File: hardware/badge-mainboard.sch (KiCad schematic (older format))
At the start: 34 parts, among them J1 Vin, J3 Rpi_02x20_WaveShareEPD, J4 I2C_HEADER, J5 I2C_HEADER, SW1 User Button 2, SW2 User Button 1, SW3 User Button 3, SW4 User Button 4, U1 LM1117-3.3, U2 sensor-module-board

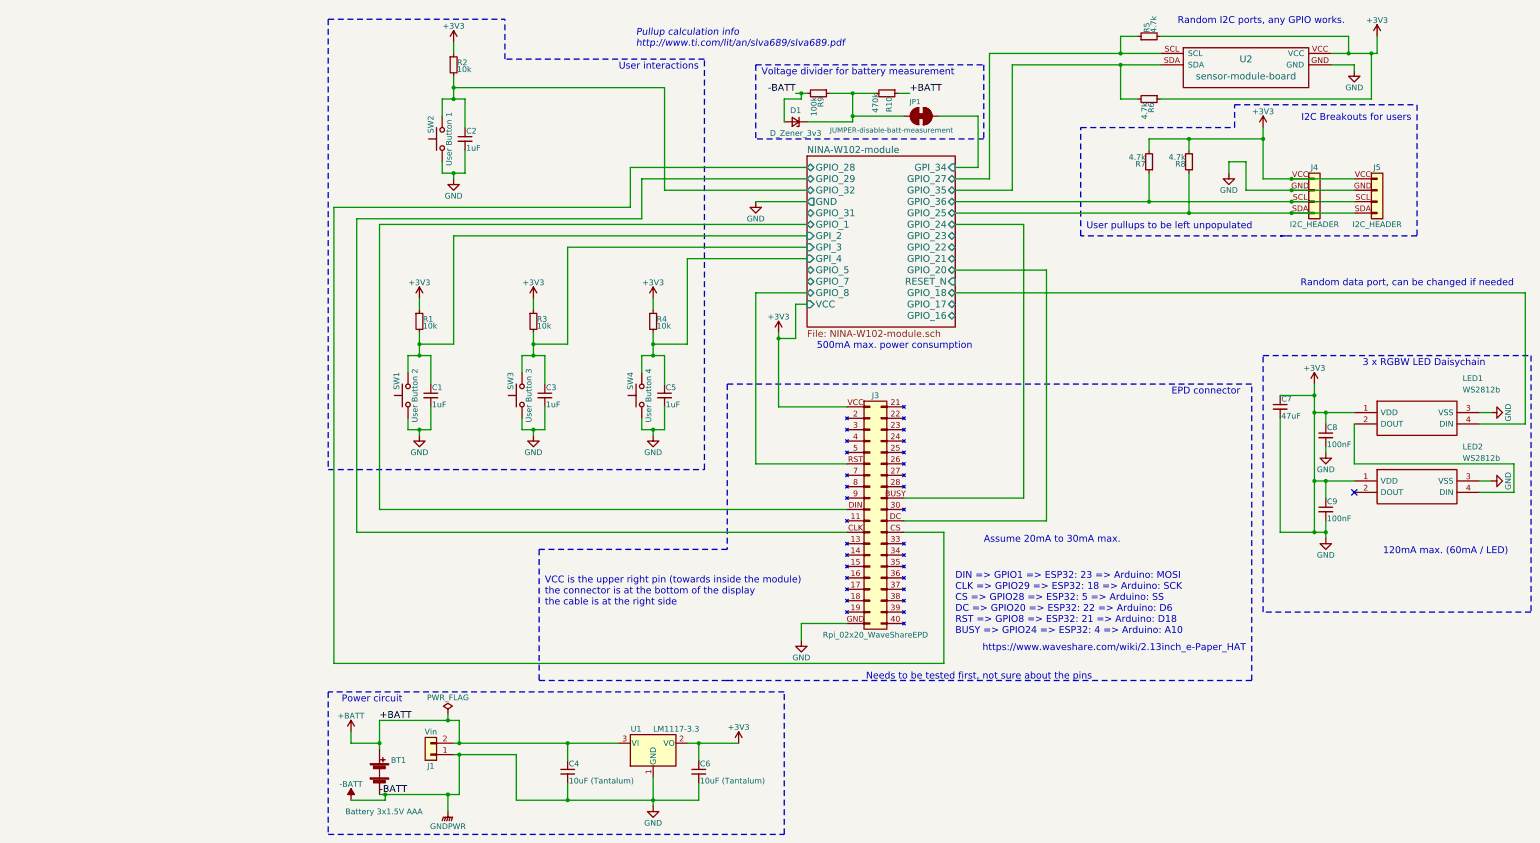
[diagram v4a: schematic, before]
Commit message: Fix 3v3 to GND connection on `ws28b`
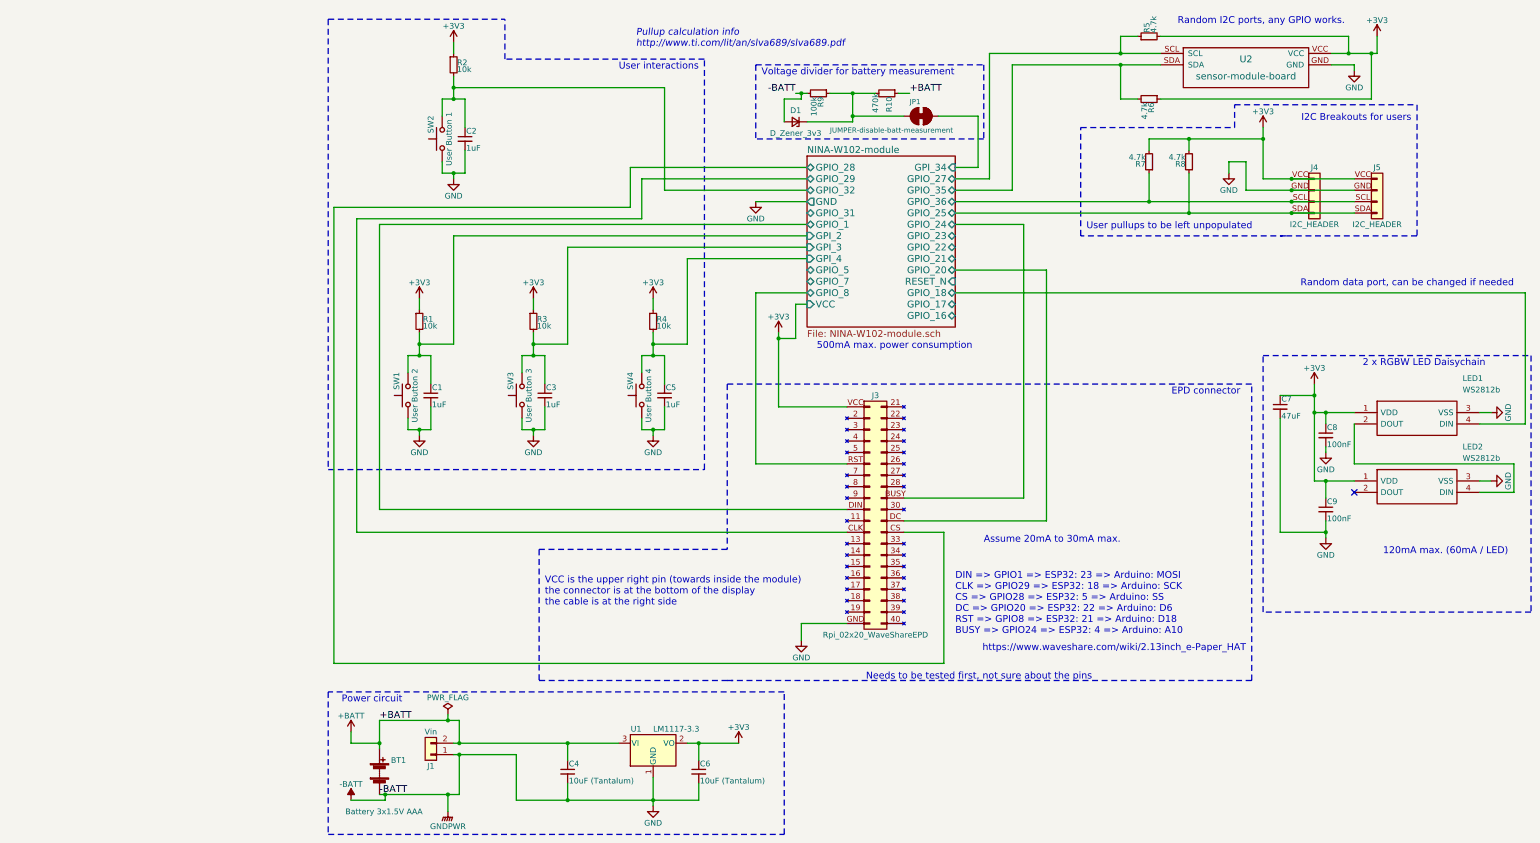
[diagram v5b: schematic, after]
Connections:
- net +3V3: no longer BT1.2 (-), C1.2, C2.2, C3.2, C4.2, C5.2, C6.2, C7.2, C8.2, C9.2, D1.2 (A), J1.1 (Pin_1), J3.GND (Pin_20), J4.GND, J5.GND, LED1.3 (VSS), LED2.3 (VSS), R9.2, SW1.1, SW2.1, SW3.1, SW4.1, U1.1 (GND), U2.GND
- new net -BATT: BT1.2 (-), C1.2, C2.2, C3.2, C4.2, C5.2, C6.2, C7.2, C8.2, C9.2, D1.2 (A), J1.1 (Pin_1), J3.GND (Pin_20), J4.GND, J5.GND, LED1.3 (VSS), LED2.3 (VSS), R9.2, SW1.1, SW2.1, SW3.1, SW4.1, U1.1 (GND), U2.GND
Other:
- note added: "2 x RGBW LED Daisychain"
- note removed: "3 x RGBW LED Daisychain"
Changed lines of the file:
@@
 LIBS:badgeComponents
 LIBS:badge-mainboard-cache
-EELAYER 25 0
+EELAYER 26 0
 EELAYER END
 $Descr A4 11693 8268
@@
 $EndComp
 Text Notes 10750 3600 2    60   ~ 0
-3 x RGBW LED Daisychain
+2 x RGBW LED Daisychain
 Text Notes 8050 600  0    60   ~ 0
 Random I2C ports, any GPIO works.
@@
 	9250 4600 9600 4600
 Connection ~ 9250 4000
-Connection ~ 9250 4600
 Wire Wire Line
 	9350 4300 9350 4350
@@
 	9600 950  9600 1000
 Wire Wire Line
-	9800 700  9800 850
-Wire Wire Line
-	9800 850  9400 850
+	9800 850  9800 700
+Wire Wire Line
+	9400 850  9800 850
 Wire Wire Line
 	6400 850  7900 850
@@
 	1700 6900 3150 6900
 Wire Wire Line
-	1750 6900 1750 6700
-Wire Wire Line
-	1750 6700 1050 6700
+	1750 6700 1750 6900
+Wire Wire Line
+	1050 6700 1750 6700
 Connection ~ 1750 6900
 Wire Notes Line
@@
 	8950 5050 9350 5050
 Wire Wire Line
-	9250 3750 9250 5050
+	9250 3750 9250 4600
 Wire Wire Line
 	9350 4950 9350 5100
@@
 Wire Wire Line
 	8950 4050 8950 5050
-Connection ~ 9250 5050
 Wire Wire Line
 	6100 2750 6900 2750
@@
 	1600 1250 1800 1250
 Wire Wire Line
-	1700 1250 1700 1050
+	1700 1050 1700 1250
 Wire Wire Line
 	1800 1250 1800 1500
@@
 	1300 3500 1500 3500
 Wire Wire Line
-	1400 3500 1400 3300
+	1400 3300 1400 3500
 Wire Wire Line
 	1500 3500 1500 3750
@@
 	2300 3500 2500 3500
 Wire Wire Line
-	2400 3500 2400 3300
+	2400 3300 2400 3500
 Wire Wire Line
 	2500 3500 2500 3750
@@
 	3350 3500 3550 3500
 Wire Wire Line
-	3450 3500 3450 3300
+	3450 3300 3450 3500
 Wire Wire Line
 	3550 3500 3550 3750
@@
 	5600 1200 5700 1200
 Wire Wire Line
-	4800 1200 4700 1200
+	4700 1200 4800 1200
 Wire Notes Line
 	4350 950  4350 1600

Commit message: Added diode and cleanedup shematic
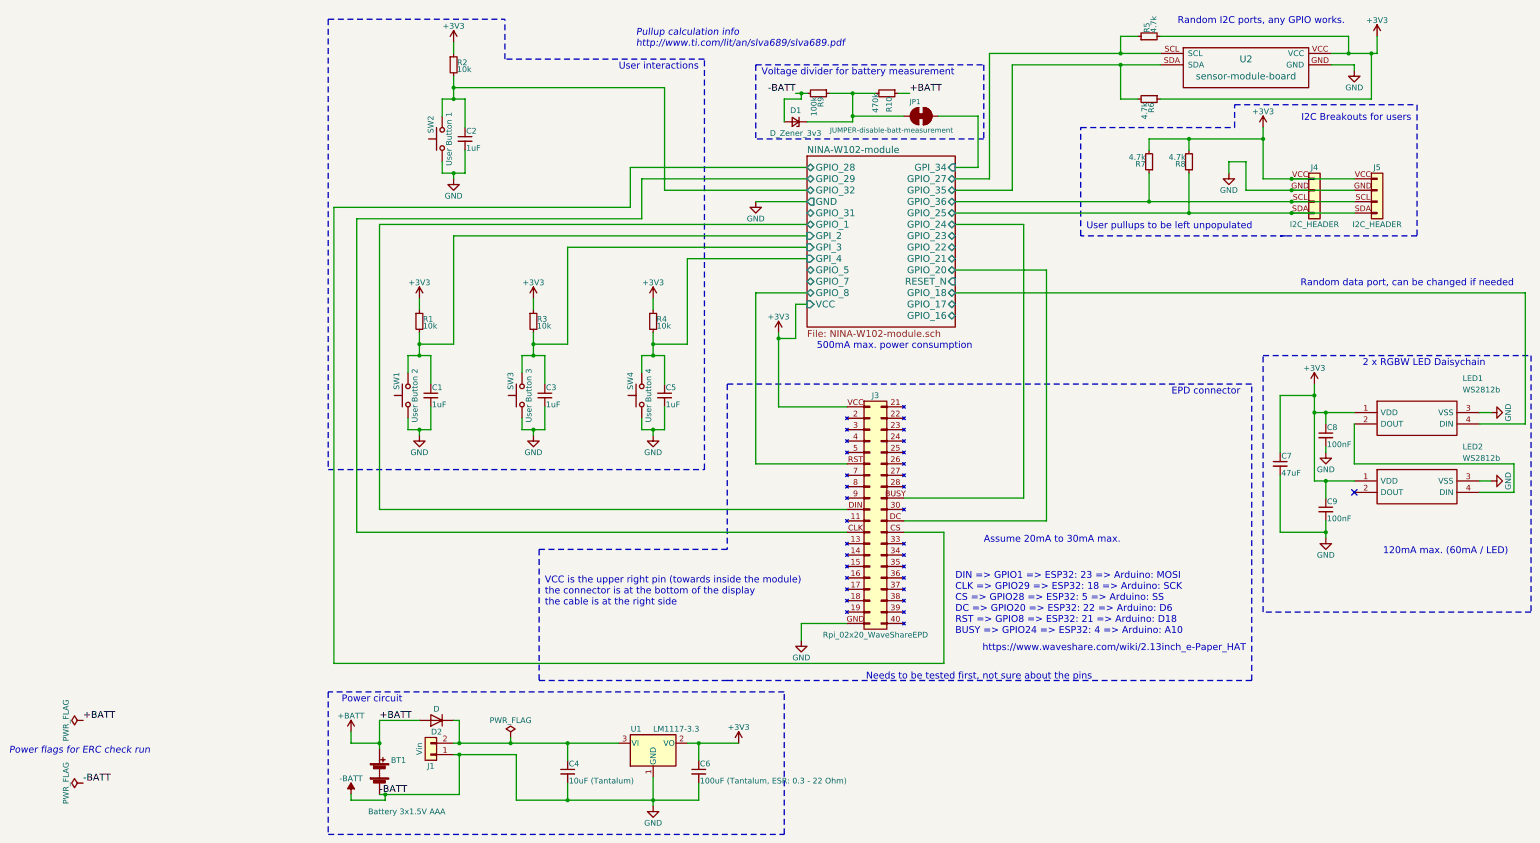
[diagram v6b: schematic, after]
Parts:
- added D2: D, Diodes_SMD:D_1206, symbol D
- C1, C2, C3, C5, C7, C8, C9: footprint Capacitors_SMD:C_1206 -> Capacitors_SMD:C_1206_HandSoldering
- C4: footprint Capacitors_SMD:C_1206 -> Capacitors_Tantalum_SMD:CP_Tantalum_Case-C_EIA-6032-28_Hand
- C6: value 10uF (Tantalum) -> 100uF (Tantalum, ESR: 0.3 - 22 Ohm); footprint Capacitors_SMD:C_1206 -> Capacitors_Tantalum_SMD:CP_Tantalum_Case-C_EIA-6032-28_Hand
- R1, R10, R2, R3, R4, R5, R6, R9: footprint Resistors_SMD:R_1206 -> Resistors_SMD:R_1206_HandSoldering
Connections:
- net +BATT: now also D2.2 (A); no longer C4.1, J1.2 (Pin_2), U1.3 (VI)
- new net: C4.1, D2.1 (K), J1.2 (Pin_2), U1.3 (VI)
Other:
- note added: "Power flags for ERC check run"
- moved on the sheet: C7

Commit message: Added comments for BOM
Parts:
- C4: Description (none) -> Tantalum
- C6: Description (none) -> Tantalum with ESR between 0.3 Ohm and 22 Ohm
- R7, R8: Description (none) -> User pullups, leave unpopulated
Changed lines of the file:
@@
 F 2 "Resistors_SMD:R_1206_HandSoldering" H 7800 1800 50  0001 C CNN
 F 3 "" H 7800 1800 50  0001 C CNN
+F 4 "User pullups, leave unpopulated" H 7800 1800 60  0001 C CNN "Description"
 	1    7800 1800
 	-1   0    0    1
@@
 F 2 "Resistors_SMD:R_1206_HandSoldering" H 8150 1800 50  0001 C CNN
 F 3 "" H 8150 1800 50  0001 C CNN
+F 4 "User pullups, leave unpopulated" H 8150 1800 60  0001 C CNN "Description"
 	1    8150 1800
 	-1   0    0    1
@@
 F 2 "Capacitors_Tantalum_SMD:CP_Tantalum_Case-C_EIA-6032-28_Hand" H 2700 7150 50  0001 C CNN
 F 3 "" H 2700 7150 50  0001 C CNN
+F 4 "Tantalum" H 2700 7150 60  0001 C CNN "Description"
 	1    2700 7150
 	1    0    0    -1
@@
 F 2 "Capacitors_Tantalum_SMD:CP_Tantalum_Case-C_EIA-6032-28_Hand" H 3850 7150 50  0001 C CNN
 F 3 "" H 3850 7150 50  0001 C CNN
+F 4 "Tantalum with ESR between 0.3 Ohm and 22 Ohm" H 3850 7150 60  0001 C CNN "Description"
 	1    3850 7150
 	1    0    0    -1

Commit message: added some more comments
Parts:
- J4, J5: Description (none) -> Leave unpopulated
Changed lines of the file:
@@
 F 2 "badgeComponents:I2C_HEADER_1X04_LOCK_LONGPADS" H 9250 2050 50  0001 C CNN
 F 3 "" H 9250 2050 50  0001 C CNN
+F 4 "Leave unpopulated" H 9250 2050 60  0001 C CNN "Description"
 	1    9250 2050
 	1    0    0    -1
@@
 F 2 "badgeComponents:I2C_HEADER_1X04_LOCK_LONGPADS" H 9800 2050 50  0001 C CNN
 F 3 "" H 9800 2050 50  0001 C CNN
+F 4 "Leave unpopulated" H 9800 2050 60  0001 C CNN "Description"
 	1    9800 2050
 	1    0    0    -1
